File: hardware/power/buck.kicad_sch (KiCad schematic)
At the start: 24 parts, among them U201 TPS54560

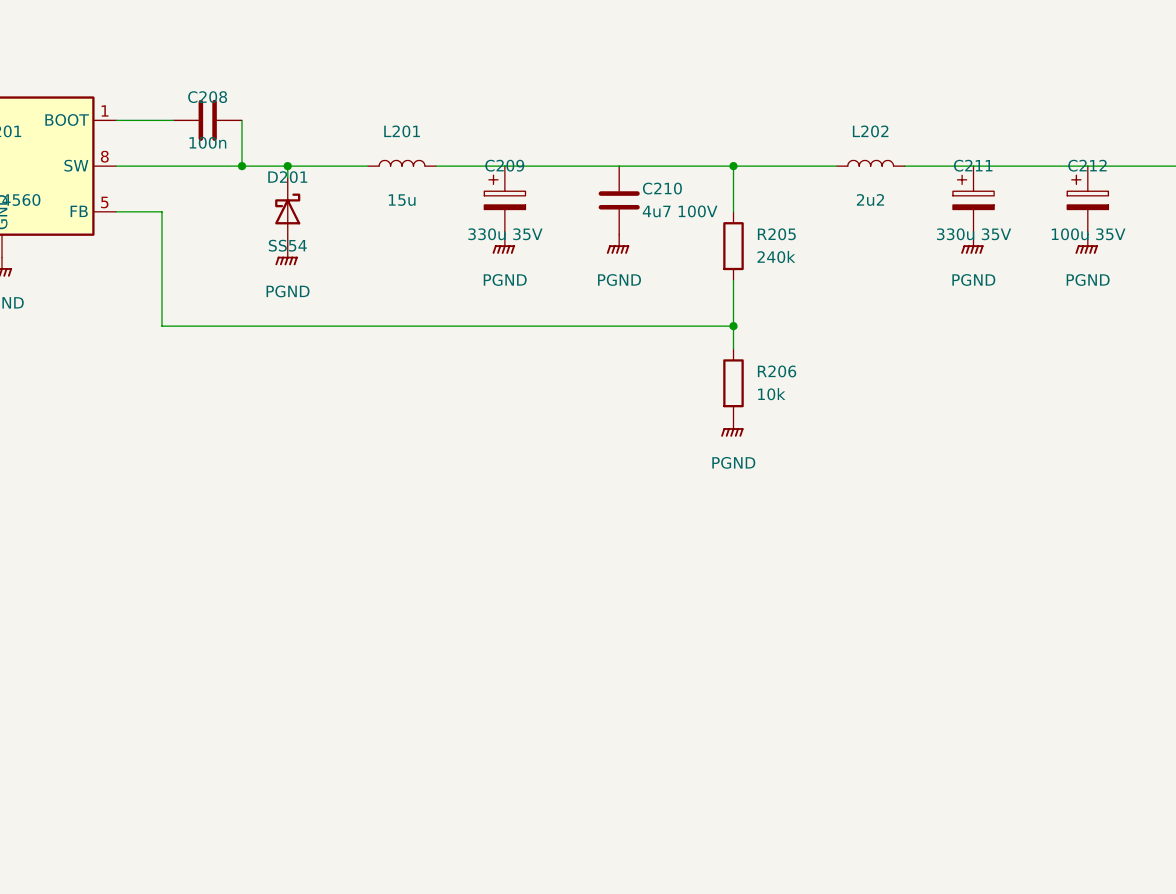
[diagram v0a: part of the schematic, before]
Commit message: Power board: confirm decision 100 values, add start-up ramp
The user confirmed the UVLO thresholds (21.1 / 18.7 V), the oscillator
(4.7 k / 560 p), the switch and LED at the rear edge and the L / F
part-number categories.

An averaged ngspice model (scripts/startup_sim.py) showed the fixed
2.6 ms soft-start into about 1.1 mF per rail takes 183-262 W from the
brick, over the GSM120B24's 126 W hiccup threshold. Each converter now
gets 47 nF from its output through a 1N4148W into FB (1 M and a clamp
diode reset the node): the rails rise with tau 11.3 ms and the input
peaks at about 54 W. Netlist checks 0 problems, ERC 0/0.

Co-Authored-By: Claude Opus 5.5 <noreply@anthropic.com>
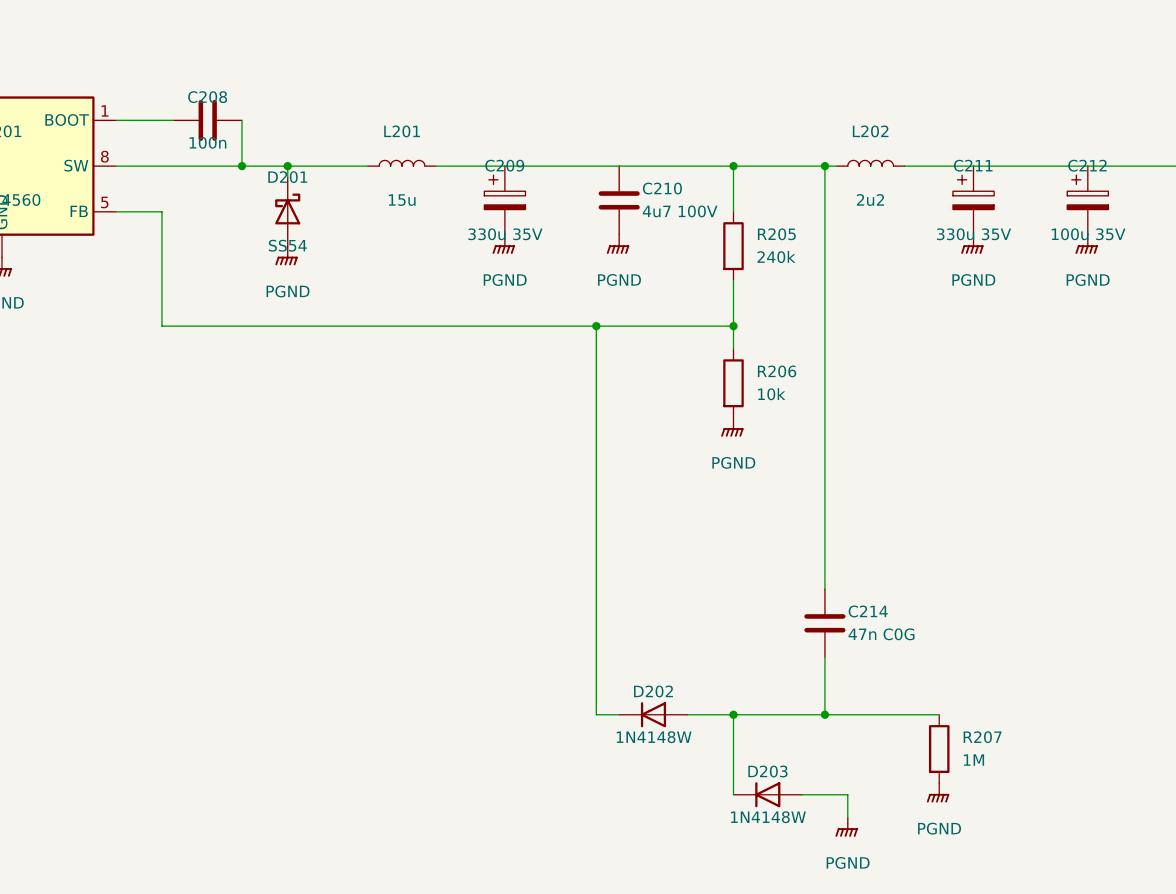
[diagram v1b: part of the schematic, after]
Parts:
- added C214: 47n C0G, Capacitor_SMD:C_0805_2012Metric, symbol Device:C
- added D202, D203: 1N4148W, Diode_SMD:D_SOD-123, symbol Device:D
- added R207: 1M, Resistor_SMD:R_0805_2012Metric, symbol Device:R
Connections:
- net PGND: now also D203.2 (A), R207.2
- net at C209.1, C210.1, L201.2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: now also C214.1
- net at R205.2, R206.1, U201.5 (FB): now also D202.1 (K)
- new net: C214.2, D202.2 (A), D203.1 (K), R207.1

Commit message: Power board: E24 dividers, rear-panel rocker, last parts chosen (decisions 156-159)
- 156: UVLO 680k/39k (start 21.3 V, stop 19.0 V), RT 240k, buck
  compensation 16k; design.py and startup_sim.py rerun (start-up unchanged,
  GSM220B24 limit in the model)
- 157: power switch a Legion SS11-BBIWG-R20-R rocker on the rear panel,
  wired to J102 (JST XH 2-pin) in place of SW101; counted in costs.py
- 158: C103 Nichicon UHE1H101MPD radial; sync caps 10 pF C0G 50 V 0603
- 159: D201 SS54 on D_SMA to match LCSC C22452
- Netlist checks 0 problems, ERC 0/0; estimate 764/1045/1641 EUR
  (4/8/16 ch), 28 fee types

Co-Authored-By: Claude Opus 5.5 <noreply@anthropic.com>
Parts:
- C207: value 10p C0G 100V -> 10p C0G; footprint Capacitor_SMD:C_0805_2012Metric -> Capacitor_SMD:C_0603_1608Metric; MPN (none) -> CL10C100JB8NNNC; Manufacturer (none) -> Samsung Electro-Mechanics; ProjectPN SX-C-022 -> SX-C-029; Supplier (none) -> LCSC; SupplierPN (none) -> C1634
- D201: footprint Diode_SMD:D_SMC -> Diode_SMD:D_SMA
- R201: value 732k -> 680k; MPN (none) -> 0805W8F6803T5E; Manufacturer (none) -> UNI-ROYAL; ProjectPN SX-R-085 -> SX-R-036; Supplier (none) -> LCSC; SupplierPN (none) -> C17797
- R202: value 42k2 -> 39k; MPN (none) -> 0805W8F3902T5E; Manufacturer (none) -> UNI-ROYAL; ProjectPN SX-R-086 -> SX-R-104; Supplier (none) -> LCSC; SupplierPN (none) -> C25826
- R203: value 15k8 -> 16k; MPN (none) -> 0805W8F1602T5E; Manufacturer (none) -> UNI-ROYAL; ProjectPN SX-R-029 -> SX-R-005; Supplier (none) -> LCSC; SupplierPN (none) -> C17490
- R204: value 243k -> 240k; ProjectPN SX-R-083 -> SX-R-084

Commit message: Power board: PCB placed and routed by scripts, panel-mount brick jack, small module without chain 2 (decisions 182, 185, 186)
Co-Authored-By: Claude Opus 5.5 <noreply@anthropic.com>
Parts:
- L201: footprint (none) -> syntsamix:L_Bourns_SRP1265A; Note Footprint to draw from the maker's drawing at PCB layout -> (none)
- U201: footprint Package_SO:Texas_R-PDSO-G8_EP2.95x4.9mm_Mask2.4x3.1mm_ThermalVias -> Package_SO:Texas_R-PDSO-G8_EP2.95x4.9mm_Mask2.4x3.1mm
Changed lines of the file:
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@@
 			)
 		)
-		(property "Footprint" ""
+		(property "Footprint" "syntsamix:L_Bourns_SRP1265A"
 			(at 196.85 127 90)
 			(hide yes)
@@
 		)
 		(property "SupplierPN" "C189912"
-			(at 196.85 127 0)
-			(hide yes)
-			(show_name no)
-			(do_not_autoplace no)
-			(effects
-				(font
-					(size 1.27 1.27)
-				)
-			)
-		)
-		(property "Note" "Footprint to draw from the maker's drawing at PCB layout"
 			(at 196.85 127 0)
 			(hide yes)
@@
 			)
 		)
-		(property "Footprint" "Package_SO:Texas_R-PDSO-G8_EP2.95x4.9mm_Mask2.4x3.1mm_ThermalVias"
+		(property "Footprint" "Package_SO:Texas_R-PDSO-G8_EP2.95x4.9mm_Mask2.4x3.1mm"
 			(at 152.4 127 0)
 			(hide yes)

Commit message: Power board: DNP switch-node RC snubber footprints across D201 and D301, bench EMI checklist (decision 189)
R208/C215 (SW to PGND, above D201) and R308/C315 (SW to -20V_CONV, beside
D301), 0805, not fitted: values from a bench measurement of the ringing on the
first boards ("Bench, first boards" in CHECKLISTS.md, with the input filter
check of decision 187). placement.py takes DNP and BOM flags from the symbols.
ERC 0/0, DRC 0, parity clean; cost unchanged.

Co-Authored-By: Claude Opus 5.5 <noreply@anthropic.com>
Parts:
- added C215: 470p 100V, Capacitor_SMD:C_0805_2012Metric, symbol Device:C
- added R208: 4R7, Resistor_SMD:R_0805_2012Metric, symbol Device:R
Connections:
- net PGND: now also C215.2
- net at C208.2, D201.1 (K), L201.1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: now also R208.1
- new net: C215.1, R208.2
